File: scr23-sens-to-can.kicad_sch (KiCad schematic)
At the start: 28 parts

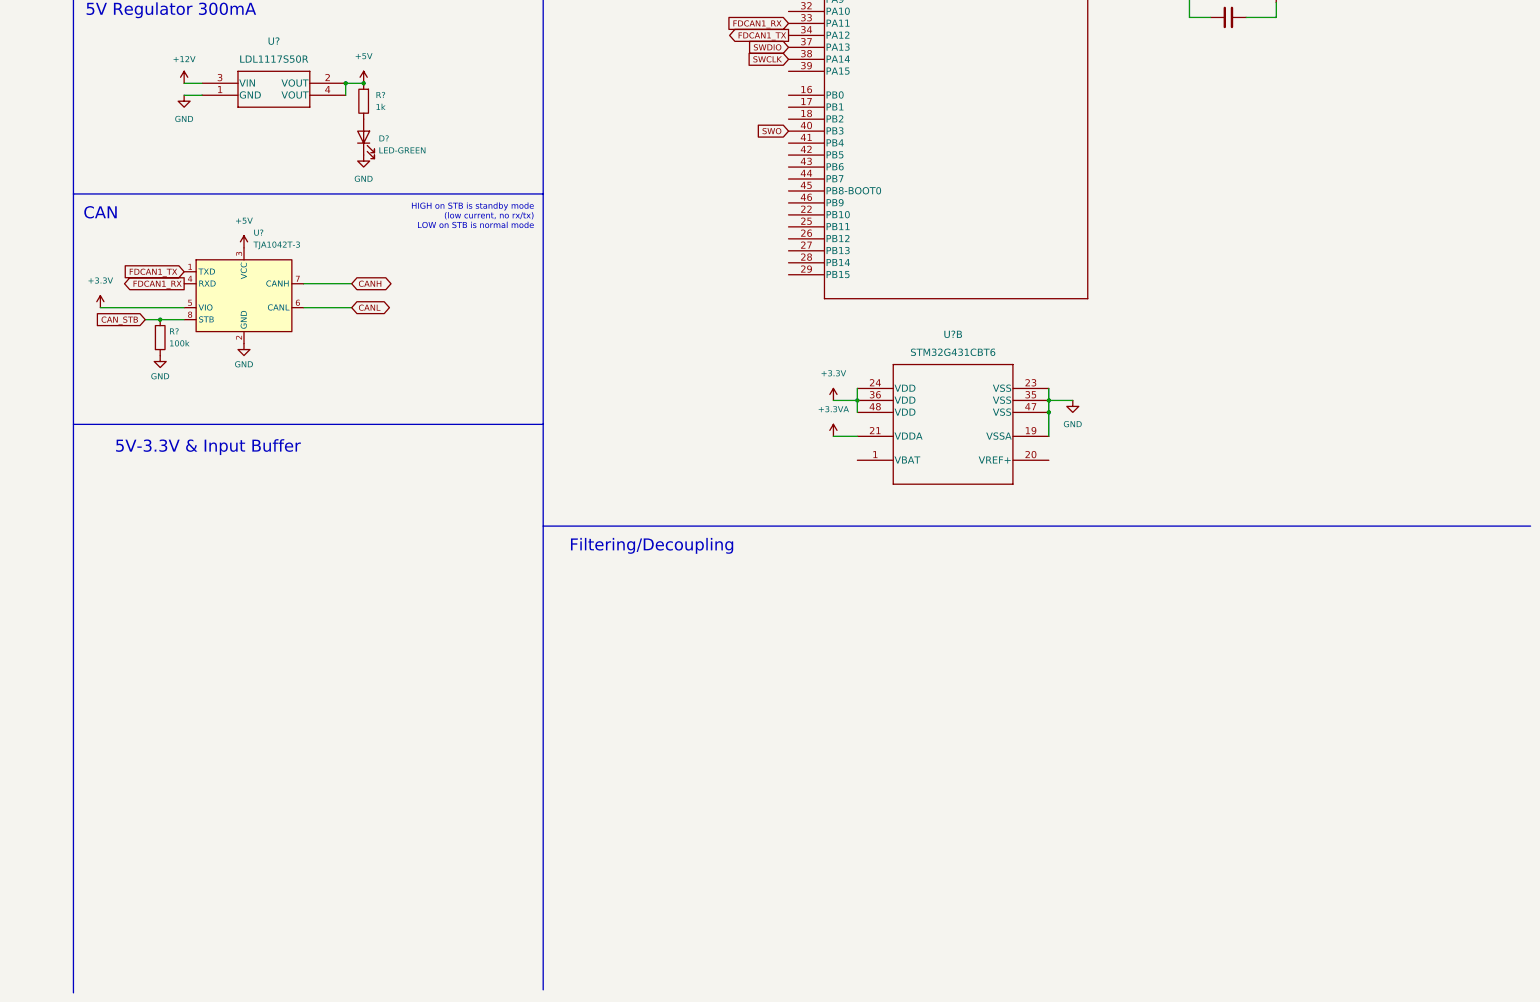
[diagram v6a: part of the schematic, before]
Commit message: add buffer circuit using lm358QT (dfn8x8) tho it's out of stock on lcsc in stock digikey
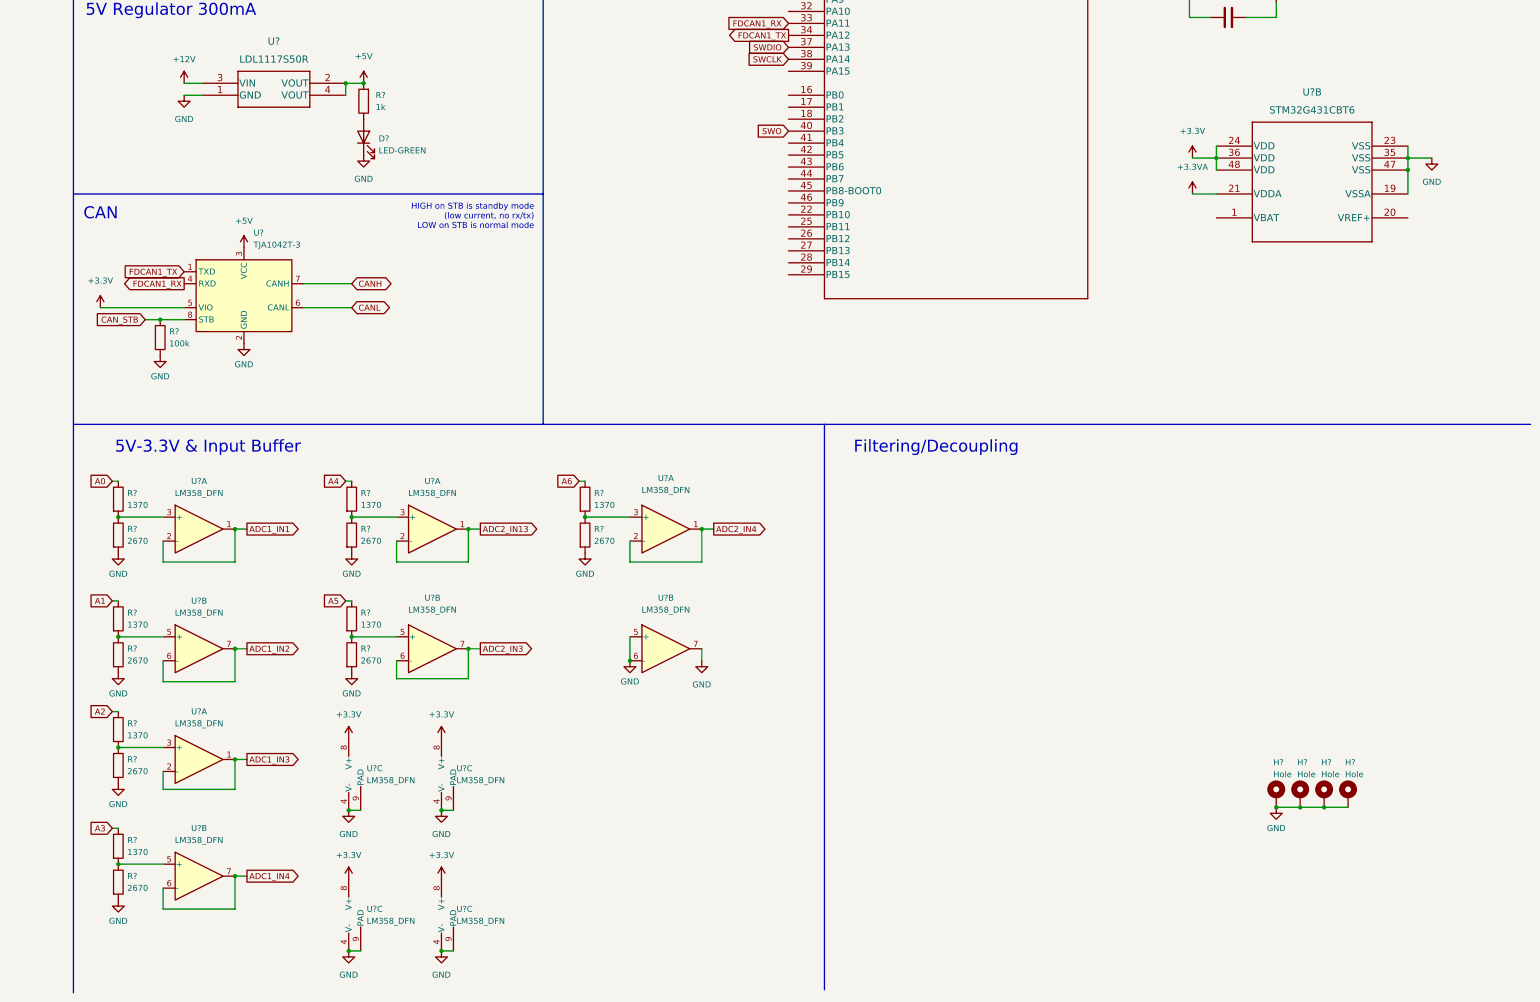
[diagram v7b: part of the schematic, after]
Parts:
- added H? (x4): Hole, symbol Mechanical:MountingHole_Pad
- added R? (x7): 2670, symbol Device:R
- added R? (x7): 1370, symbol Device:R
- added U? (x12): LM358_DFN, Package_DFN_QFN:DFN-8-1EP_2x2mm_P0.5mm_EP1.05x1.75mm, symbol Amplifier_Operational:LM358_DFN
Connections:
- net +3.3V: now also U?.8 (V+), U?.8 (V+), U?.8 (V+), U?.8 (V+)
- net A0: now also R?.1
- net A1: now also R?.1
- net A2: now also R?.1
- net A3: now also R?.1
- net A4: now also R?.1
- net A5: now also R?.1
- net A6: now also R?.1
- net ADC1_IN1: now also U?.1, U?.2 (-)
- net ADC1_IN2: now also U?.6 (-), U?.7
- net ADC1_IN3: now also U?.1, U?.2 (-)
- net ADC1_IN4: now also U?.6 (-), U?.7
- net ADC2_IN13: now also U?.1, U?.2 (-)
- net ADC2_IN3: now also U?.6 (-), U?.7
- net ADC2_IN4: now also U?.1, U?.2 (-)
- net GND: now also H?.1, H?.1, H?.1, H?.1, R?.2, R?.2, R?.2, R?.2, R?.2, R?.2, R?.2, U?.4 (V-), U?.4 (V-), U?.4 (V-), U?.4 (V-), U?.5 (+), U?.6 (-), U?.7, U?.9 (PAD), U?.9 (PAD), U?.9 (PAD), U?.9 (PAD)
- new net: R?.1, R?.2, U?.3 (+) (x4)
- new net: R?.1, R?.2, U?.5 (+) (x3)
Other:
- moved on the sheet: U?B

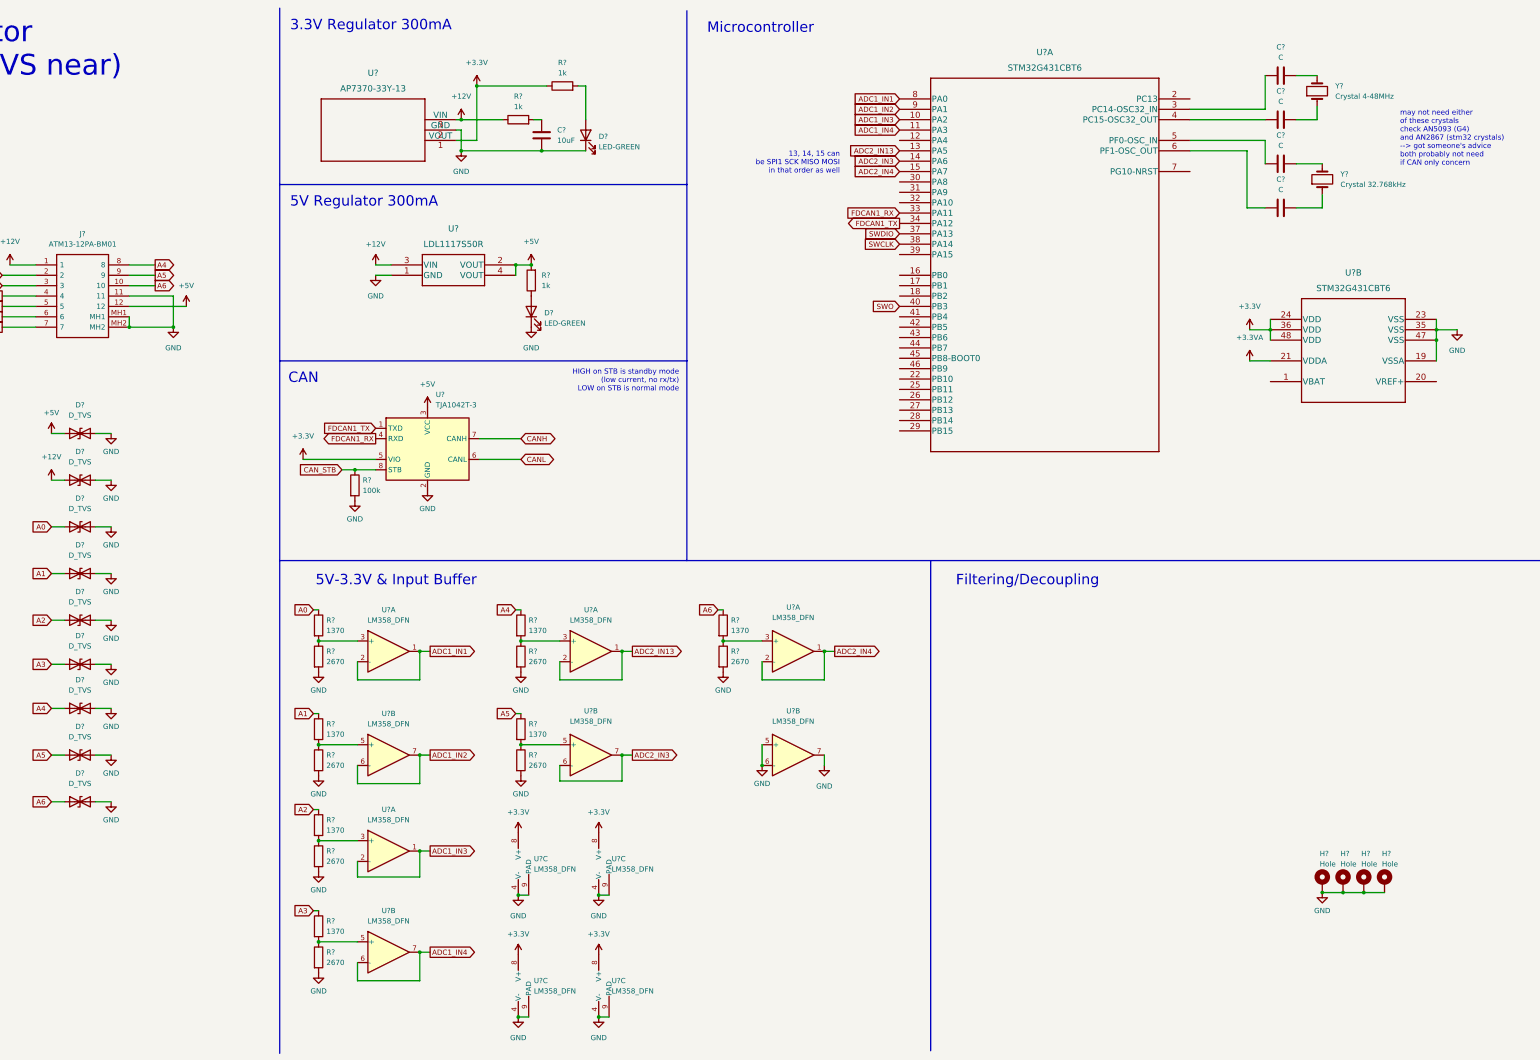
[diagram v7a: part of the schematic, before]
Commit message: add hella caps and fix odds and ends + numbering
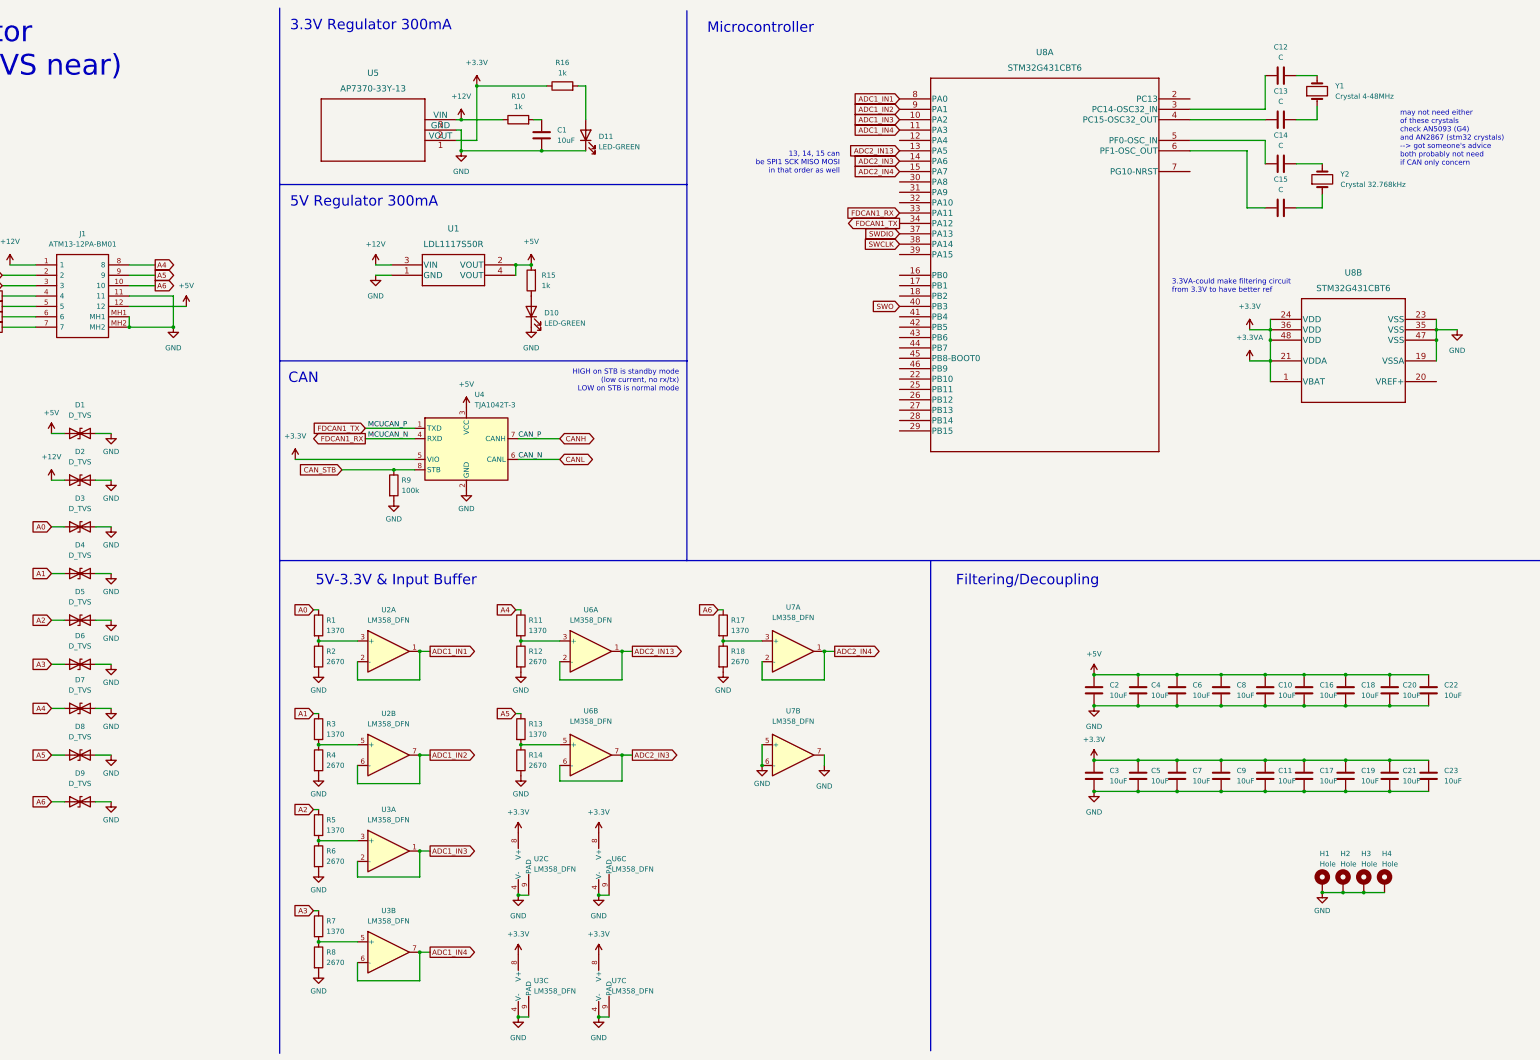
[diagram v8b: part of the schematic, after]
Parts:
- added C10, C11, C16, C17, C18, C19, C2, C20, C21, C22, C23, C3, C4, C5, C6, C7, C8, C9: 10uF, symbol Device:C
- H1, H2, H3, H4: renamed from H?; footprint (none) -> MountingHole:MountingHole_3.5mm_Pad_TopBottom
- gave numbers to parts that had none: 45
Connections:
- net +3.3VA is gone; now on net +3.3V: U8.21 (VDDA)
- net +3.3V: now also U8.1 (VBAT), C11.2, C17.2, C19.2, C21.2, C23.2, C3.2, C5.2, C7.2, C9.2
- net +5V: now also C10.2, C16.2, C18.2, C2.2, C20.2, C22.2, C4.2, C6.2, C8.2
- net GND: now also C10.1, C11.1, C16.1, C17.1, C18.1, C19.1, C2.1, C20.1, C21.1, C22.1, C23.1, C3.1, C4.1, C5.1, C6.1, C7.1, C8.1, C9.1
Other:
- note added: "3.3VA-could make filtering circuit from 3.3V to have better ref"
- moved on the sheet: R9, U4
